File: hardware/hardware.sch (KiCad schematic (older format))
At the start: 11 parts

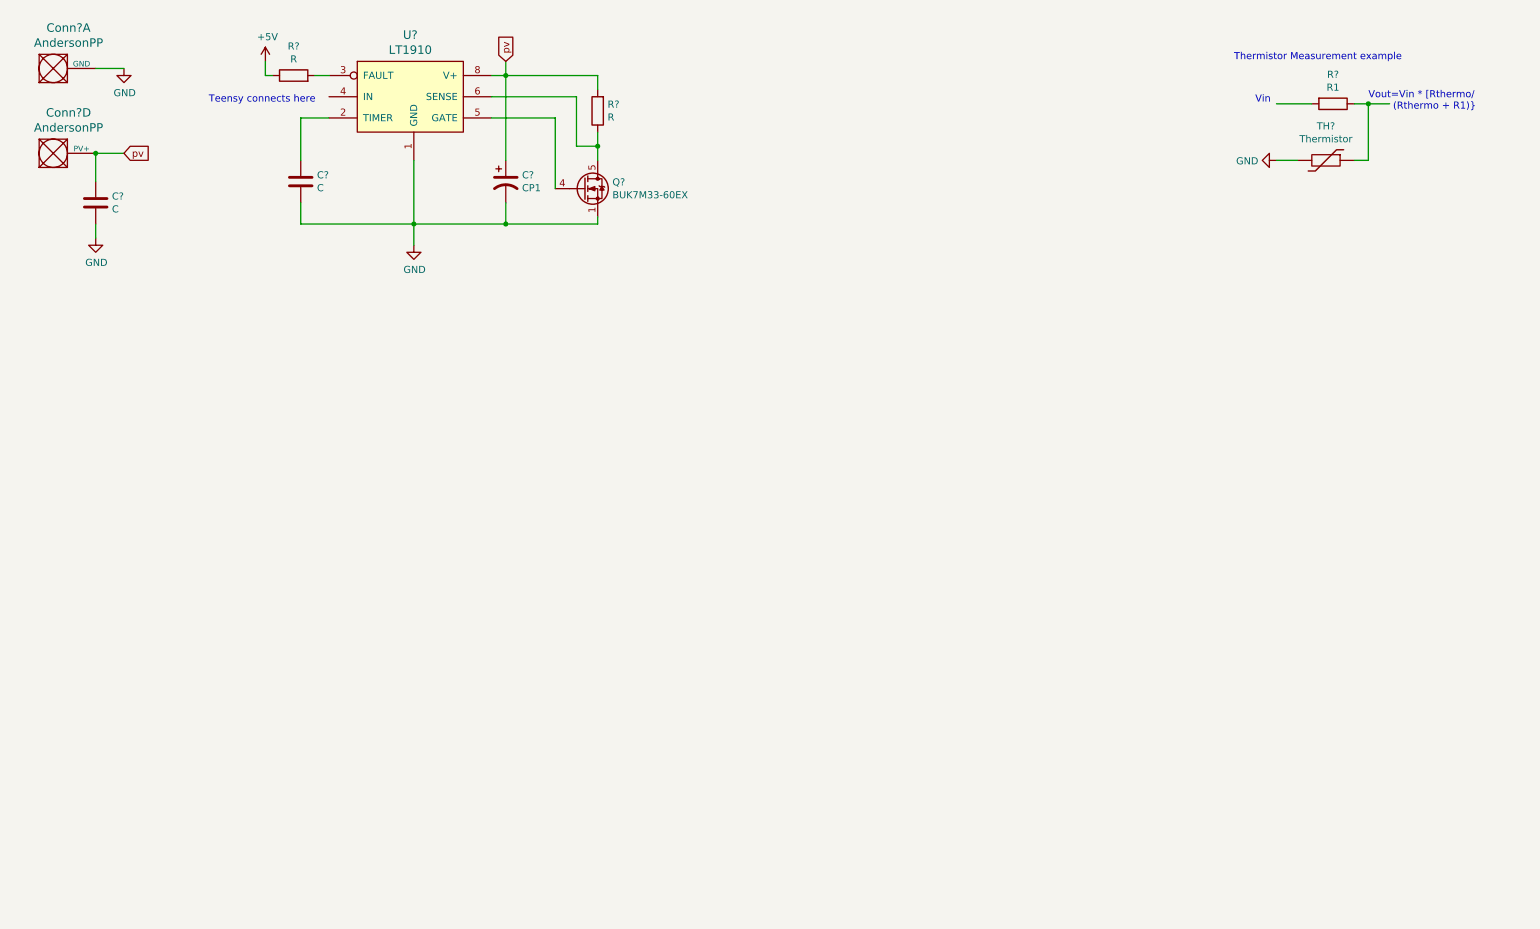
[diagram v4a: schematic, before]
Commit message: Added teensy to board and planned wire connections
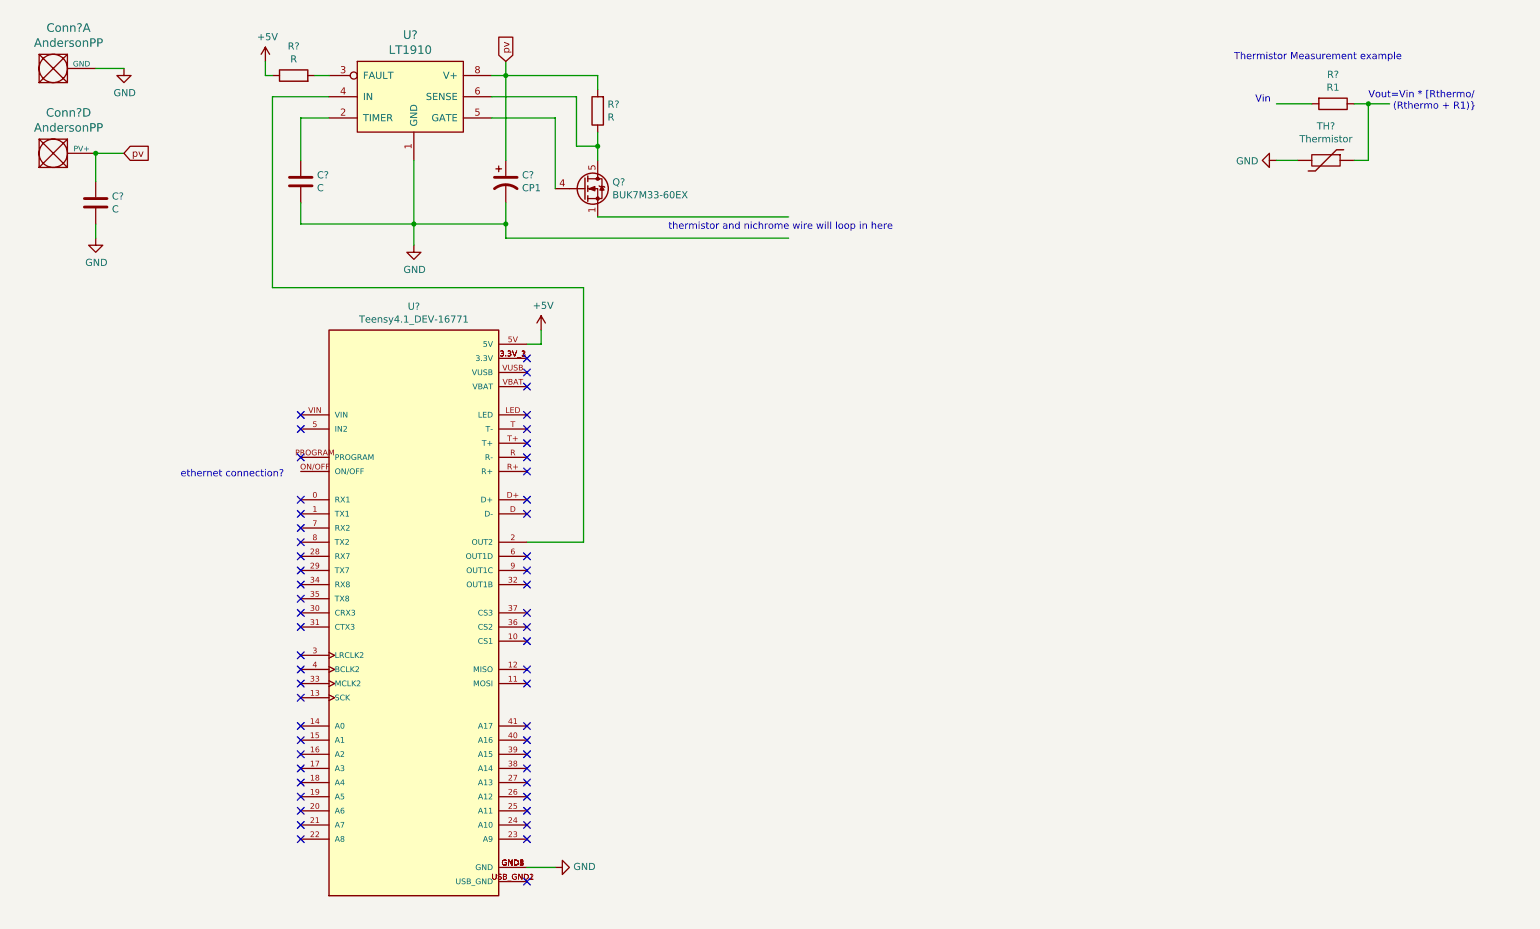
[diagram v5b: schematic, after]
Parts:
- added U?: Teensy4.1_DEV-16771, MODULE_DEV-16771, symbol MRDT_Shields:Teensy4.1_DEV-16771
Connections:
- wire segments 35 -> 44
- no-connect marks 0 -> 54
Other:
- note added: "ethernet connection?"
- note added: "thermistor and nichrome wire will loop in here"
- note removed: "Teensy connects here"
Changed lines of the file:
@@
 encoding utf-8
 Sheet 1 1
-Title ""
+Title "Heater Board"
 Date ""
 Rev ""
-Comp ""
+Comp "MRDT"
 Comment1 ""
 Comment2 ""
@@
 Wire Wire Line
 	2650 950  2750 950
-Text Notes 1900 1150 0    50   ~ 0
-Teensy connects here
 Wire Wire Line
 	3900 1100 4500 1100
@@
 	1    0    0    -1
 $EndComp
-Wire Wire Line
-	4000 2000 4650 2000
-Wire Wire Line
-	4650 2000 4650 1950
-Connection ~ 4000 2000
 $Comp
 L power:GND #PWR?
@@
 Wire Wire Line
 	3350 2150 3350 2000
+$Comp
+L MRDT_Shields:Teensy4.1_DEV-16771 U?
+U 1 1 6158A854
+P 3350 4750
+F 0 "U?" H 3350 6917 50  0000 C CNN
+F 1 "Teensy4.1_DEV-16771" H 3350 6826 50  0000 C CNN
+F 2 "MODULE_DEV-16771" H 5450 4450 50  0001 L BNN
+F 3 "" H 3350 4750 50  0001 L BNN
+F 4 "Manufacturer recommendations" H 5450 4200 50  0001 L BNN "STANDARD"
+F 5 "4.07mm" H 5700 4000 50  0001 L BNN "MAXIMUM_PACKAGE_HEIGHT"
+F 6 "SparkFun Electronics" H 5650 3850 50  0001 L BNN "MANUFACTURER"
+F 7 "4.1" H 3050 2550 50  0001 L BNN "PARTREV"
+	1    3350 4750
+	1    0    0    -1
+$EndComp
+$Comp
+L power:GND #PWR?
+U 1 1 61591C99
+P 4350 6550
+F 0 "#PWR?" H 4350 6300 50  0001 C CNN
+F 1 "GND" V 4355 6422 50  0000 R CNN
+F 2 "" H 4350 6550 50  0001 C CNN
+F 3 "" H 4350 6550 50  0001 C CNN
+	1    4350 6550
+	0    -1   -1   0
+$EndComp
+Wire Wire Line
+	4350 6550 4150 6550
+$Comp
+L power:+5V #PWR?
+U 1 1 61592E25
+P 4250 2750
+F 0 "#PWR?" H 4250 2600 50  0001 C CNN
+F 1 "+5V" H 4265 2923 50  0000 C CNN
+F 2 "" H 4250 2750 50  0001 C CNN
+F 3 "" H 4250 2750 50  0001 C CNN
+	1    4250 2750
+	1    0    0    -1
+$EndComp
+Wire Wire Line
+	4250 2750 4250 2850
+Wire Wire Line
+	4250 2850 4150 2850
+Wire Wire Line
+	4150 4250 4550 4250
+Wire Wire Line
+	4550 4250 4550 2450
+Wire Wire Line
+	4550 2450 2350 2450
+Wire Wire Line
+	2350 2450 2350 1100
+Wire Wire Line
+	2350 1100 2750 1100
+Wire Wire Line
+	4650 1950 6000 1950
+Wire Wire Line
+	4000 2000 4000 2100
+Wire Wire Line
+	4000 2100 6000 2100
+Connection ~ 4000 2000
+NoConn ~ 4150 2950
+NoConn ~ 4150 3050
+NoConn ~ 4150 3150
+NoConn ~ 4150 3350
+NoConn ~ 4150 3450
+NoConn ~ 4150 3550
+NoConn ~ 4150 3650
+NoConn ~ 4150 3750
+NoConn ~ 4150 3950
+NoConn ~ 4150 4050
+NoConn ~ 4150 4350
+NoConn ~ 4150 4450
+NoConn ~ 4150 4550
+NoConn ~ 4150 4750
+NoConn ~ 4150 4850
+NoConn ~ 4150 4950
+NoConn ~ 4150 5150
+NoConn ~ 4150 5250
+NoConn ~ 4150 5550
+NoConn ~ 4150 5650
+NoConn ~ 4150 5750
+NoConn ~ 4150 5850
+NoConn ~ 4150 5950
+NoConn ~ 4150 6050
+NoConn ~ 4150 6150
+NoConn ~ 4150 6250
+NoConn ~ 4150 6350
+NoConn ~ 4150 6650
+NoConn ~ 2550 6350
+NoConn ~ 2550 6250
+NoConn ~ 2550 6150
+NoConn ~ 2550 6050
+NoConn ~ 2550 5950
+NoConn ~ 2550 5850
+NoConn ~ 2550 5750
+NoConn ~ 2550 5650
+NoConn ~ 2550 5550
+NoConn ~ 2550 5350
+NoConn ~ 2550 5250
+NoConn ~ 2550 5150
+NoConn ~ 2550 5050
+NoConn ~ 2550 4850
+NoConn ~ 2550 4750
+NoConn ~ 2550 4650
+NoConn ~ 2550 4550
+NoConn ~ 2550 4450
+NoConn ~ 2550 4350
+NoConn ~ 2550 4250
+NoConn ~ 2550 4150
+NoConn ~ 2550 4050
+NoConn ~ 2550 3950
+NoConn ~ 2550 3350
+NoConn ~ 2550 3450
+NoConn ~ 2550 3650
+Text Notes 1700 3800 0    50   ~ 0
+ethernet connection?
+Text Notes 5150 2050 0    50   ~ 0
+thermistor and nichrome wire will loop in here
 $EndSCHEMATC

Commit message: Added thermistor measurement system
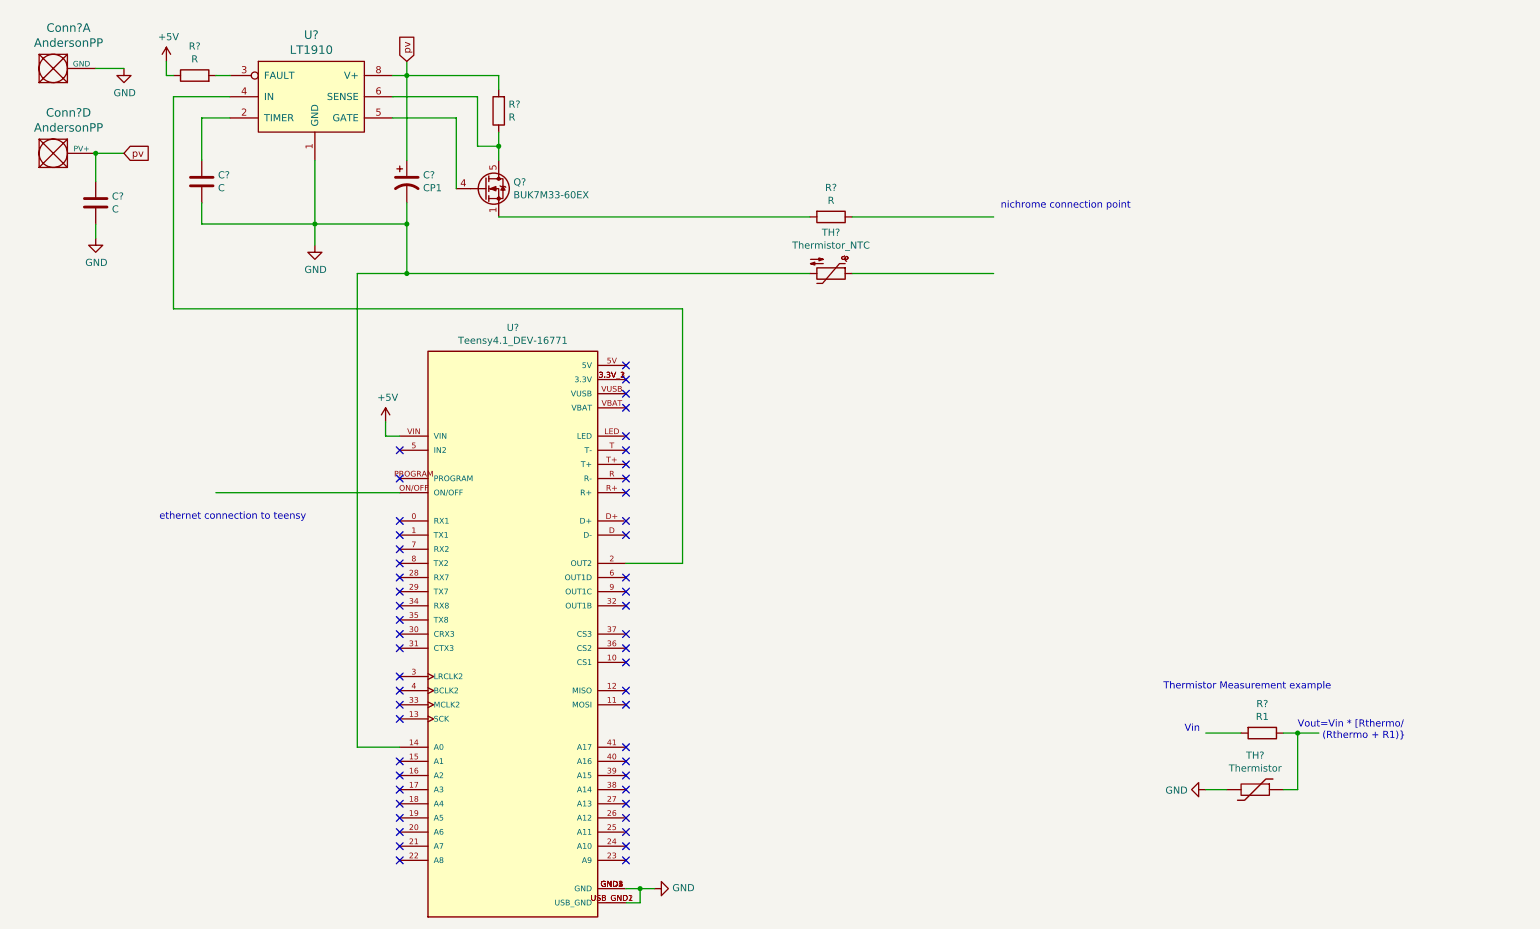
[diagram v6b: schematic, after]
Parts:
- added R?: R, symbol Device:R
- added TH?: Thermistor_NTC, symbol Device:Thermistor_NTC
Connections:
- wire segments 44 -> 53
- no-connect marks 54 -> 52
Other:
- note added: "ethernet connection to teensy"
- note added: "nichrome connection point"
- note removed: "ethernet connection?"
- note removed: "thermistor and nichrome wire will loop in here"
- moved on the sheet: C?, Q?, R?, TH?, U?

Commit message: Added buck convertors, labeled components, and added resistance and capacitance values
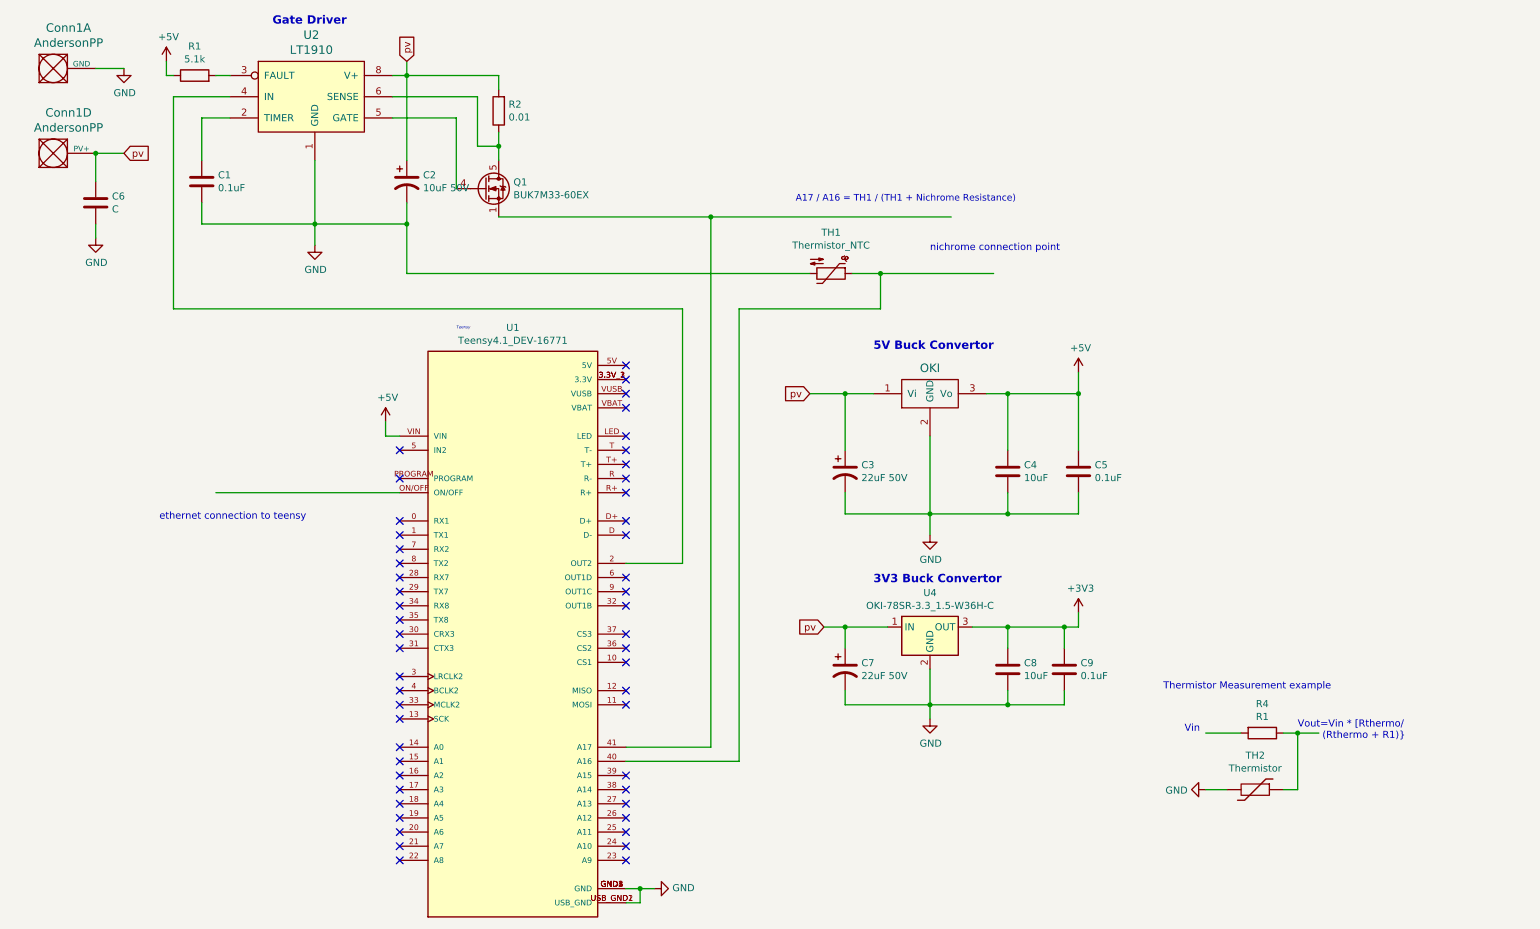
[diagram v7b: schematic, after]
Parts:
- removed R?: R, symbol Device:R
- added C3, C7: 22uF 50V, symbol Device:CP1
- added C4, C8: 10uF, symbol Device:C
- added C5, C9: 0.1uF, symbol Device:C
- added U3: OKI, symbol MRDT_Devices:OKI
- added U4: OKI-78SR-3.3_1.5-W36H-C, Converter_DCDC:Converter_DCDC_muRata_OKI-78SR_Horizontal, symbol Converter_DCDC:OKI-78SR-3.3_1.5-W36H-C
- C1: renamed from C?; value C -> 0.1uF
- C2: renamed from C?; value CP1 -> 10uF 50V
- R1: renamed from R?; value R -> 5.1k
- R2: renamed from R?; value R -> 0.01
- gave numbers to parts that had none: 8
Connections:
- net labels added: +3V3
- wire segments 53 -> 90
- no-connect marks 52 -> 51
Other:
- note added: "3V3 Buck Convertor"
- note added: "5V Buck Convertor"
- note added: "A17 / A16 = TH1 / (TH1 + Nichrome Resistance)"
- note added: "Gate Driver"
- note added: "Teensy"

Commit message: Added Current Limiter and Removed example
Gave Rmin for Thermistor and removed Comparative Resistance Circuit example
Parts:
- removed C6: C, symbol Device:C
- removed R4: R1, symbol Device:R
- removed TH2: Thermistor, symbol Device:Thermistor
- added TH3: Rmin = 840, symbol Device:Thermistor_NTC
- U1: symbol MRDT_Shields:Teensy4.1_DEV-16771 -> hardware-rescue:Teensy4.1_DEV-16771-MRDT_Shields
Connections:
- wire segments 90 -> 84
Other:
- note removed: "Thermistor Measurement example"
- note removed: "Vin"
- note removed: "Vout=Vin * [Rthermo/\n (Rthermo + R1)}"
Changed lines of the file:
@@
 Wire Wire Line
 	1300 900  1100 900
-Text GLabel 1300 1500 2    50   Input ~ 0
+Text GLabel 1200 2100 3    50   Input ~ 0
 pv
 Wire Wire Line
-	1300 1500 1100 1500
-$Comp
-L Device:C C6
-U 1 1 614D2AA6
-P 1100 1850
-F 0 "C6" H 985 1804 50  0000 R CNN
-F 1 "C" H 985 1895 50  0000 R CNN
-F 2 "" H 1138 1700 50  0001 C CNN
-F 3 "~" H 1100 1850 50  0001 C CNN
-	1    1100 1850
-	-1   0    0    1
-$EndComp
-Wire Wire Line
-	1100 1700 1100 1500
-Connection ~ 1100 1500
-Wire Wire Line
-	1100 2000 1100 2100
-$Comp
-L power:GND #PWR01
-U 1 1 614D4A55
-P 1100 2100
-F 0 "#PWR01" H 1100 1850 50  0001 C CNN
-F 1 "GND" H 1105 1927 50  0000 C CNN
-F 2 "" H 1100 2100 50  0001 C CNN
-F 3 "" H 1100 2100 50  0001 C CNN
-	1    1100 2100
-	1    0    0    -1
-$EndComp
-$Comp
-L Device:R R4
-U 1 1 614D88F5
-P 9350 5600
-F 0 "R4" V 9143 5600 50  0000 C CNN
-F 1 "R1" V 9234 5600 50  0000 C CNN
-F 2 "" V 9280 5600 50  0001 C CNN
-F 3 "~" H 9350 5600 50  0001 C CNN
-	1    9350 5600
-	0    1    1    0
-$EndComp
-Wire Wire Line
-	9600 6000 9500 6000
-$Comp
-L Device:Thermistor TH2
-U 1 1 614D97E1
-P 9300 6000
-F 0 "TH2" V 9058 6000 50  0000 C CNN
-F 1 "Thermistor" V 9149 6000 50  0000 C CNN
-F 2 "" H 9300 6000 50  0001 C CNN
-F 3 "~" H 9300 6000 50  0001 C CNN
-	1    9300 6000
-	0    1    1    0
-$EndComp
-Wire Wire Line
-	8950 6000 9100 6000
-Wire Wire Line
-	8950 5600 9200 5600
-$Comp
-L power:GND #PWR09
-U 1 1 614DAA27
-P 8950 6000
-F 0 "#PWR09" H 8950 5750 50  0001 C CNN
-F 1 "GND" V 8955 5872 50  0000 R CNN
-F 2 "" H 8950 6000 50  0001 C CNN
-F 3 "" H 8950 6000 50  0001 C CNN
-	1    8950 6000
-	0    1    1    0
-$EndComp
-Text Notes 8800 5600 0    50   ~ 0
-Vin
-Wire Wire Line
-	9500 5600 9600 5600
-Wire Wire Line
-	9600 5600 9600 6000
-Connection ~ 9600 5600
-Wire Wire Line
-	9600 5600 9750 5600
-Text Notes 9600 5650 0    50   ~ 0
-Vout=Vin * [Rthermo/\n        (Rthermo + R1)}
-Text Notes 8650 5300 0    50   ~ 0
-Thermistor Measurement example
+	1200 2100 1200 1900
 $Comp
 L MRDT_ICs:LT1910 U2
@@
 NoConn ~ 3250 5700
 $Comp
-L MRDT_Shields:Teensy4.1_DEV-16771 U1
+L hardware-rescue:Teensy4.1_DEV-16771-MRDT_Shields U1
 U 1 1 6158A854
 P 4050 4900
@@
 Text Notes 6050 1850 0    47   ~ 0
 A17 / A16 = TH1 / (TH1 + Nichrome Resistance)
+$Comp
+L Device:Thermistor_NTC TH3
+U 1 1 61610BEA
+P 1200 1750
+F 0 "TH3" H 1047 1704 50  0000 R CNN
+F 1 "Rmin = 840" H 1047 1795 50  0000 R CNN
+F 2 "" H 1200 1800 50  0001 C CNN
+F 3 "~" H 1200 1800 50  0001 C CNN
+	1    1200 1750
+	1    0    0    -1
+$EndComp
+Wire Wire Line
+	1100 1500 1200 1500
+Wire Wire Line
+	1200 1500 1200 1600
 $EndSCHEMATC
